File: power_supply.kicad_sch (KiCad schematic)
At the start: 48 parts, among them J1 USB_C_Receptacle_USB2.0, Q2 IRLR3110ZTRPBF, Q3 BSR92P, Q4 BSR92P, Q5 BSS131, Q6 BSS131, Q7 BSS131, Q8 BSS131, U1 LT3757AEMSE, U2 AMS1117-3.3

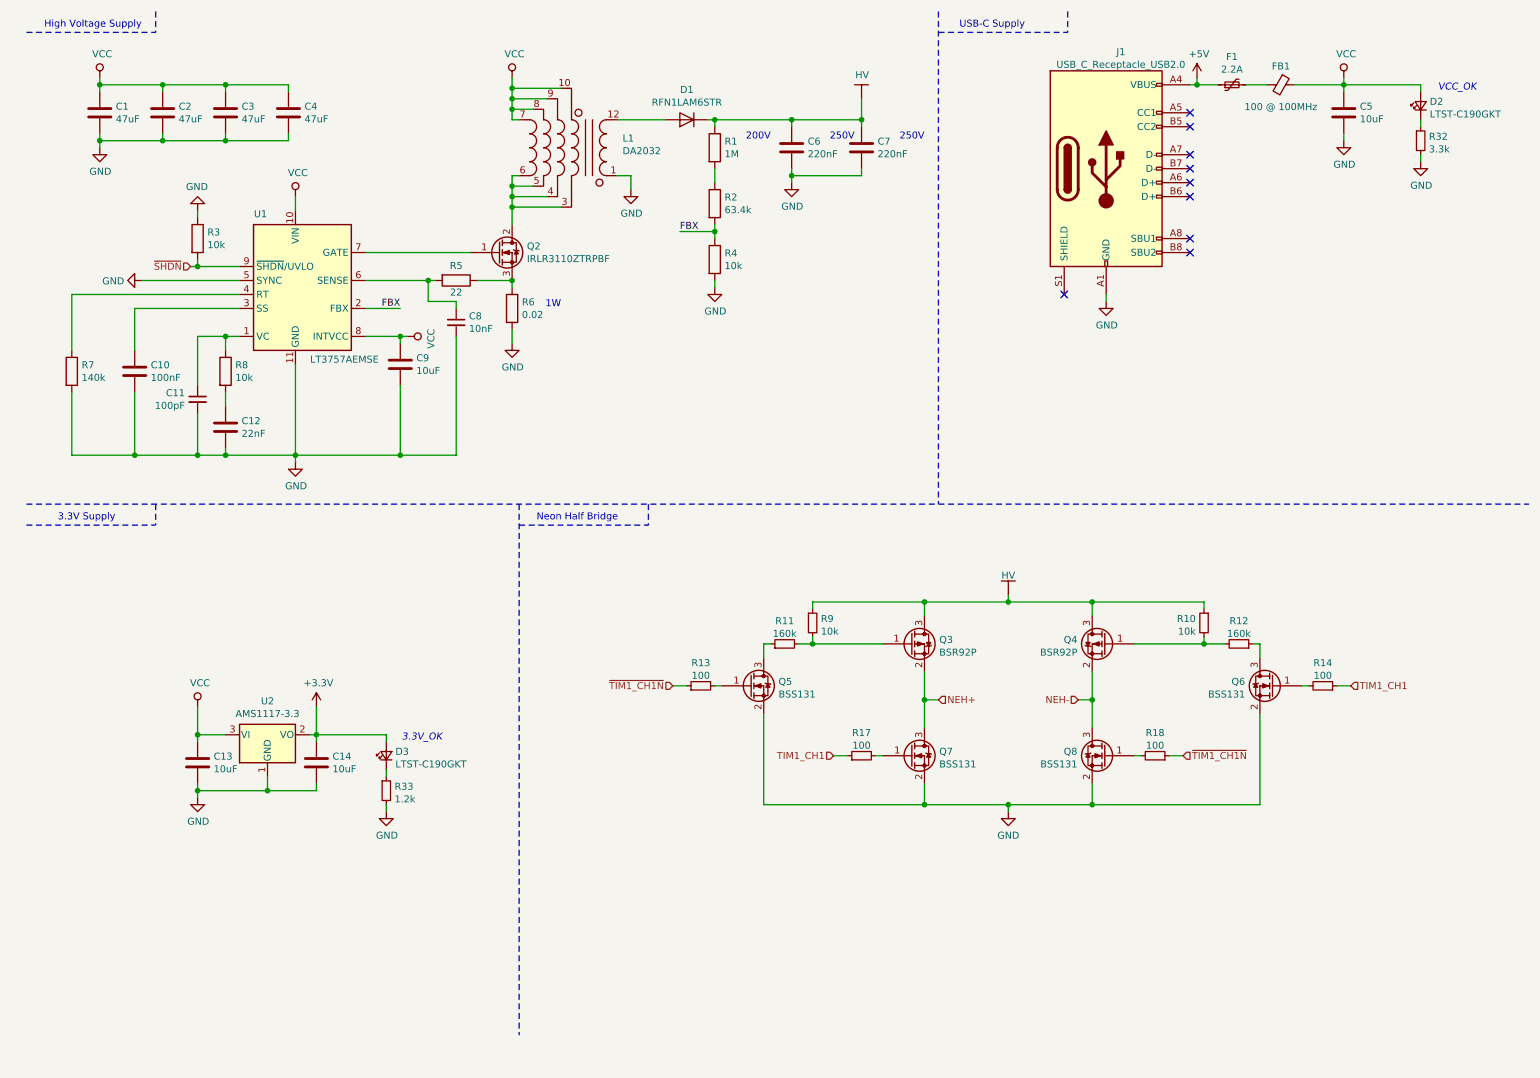
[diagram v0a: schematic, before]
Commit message: added outputs for schematic and gerber view
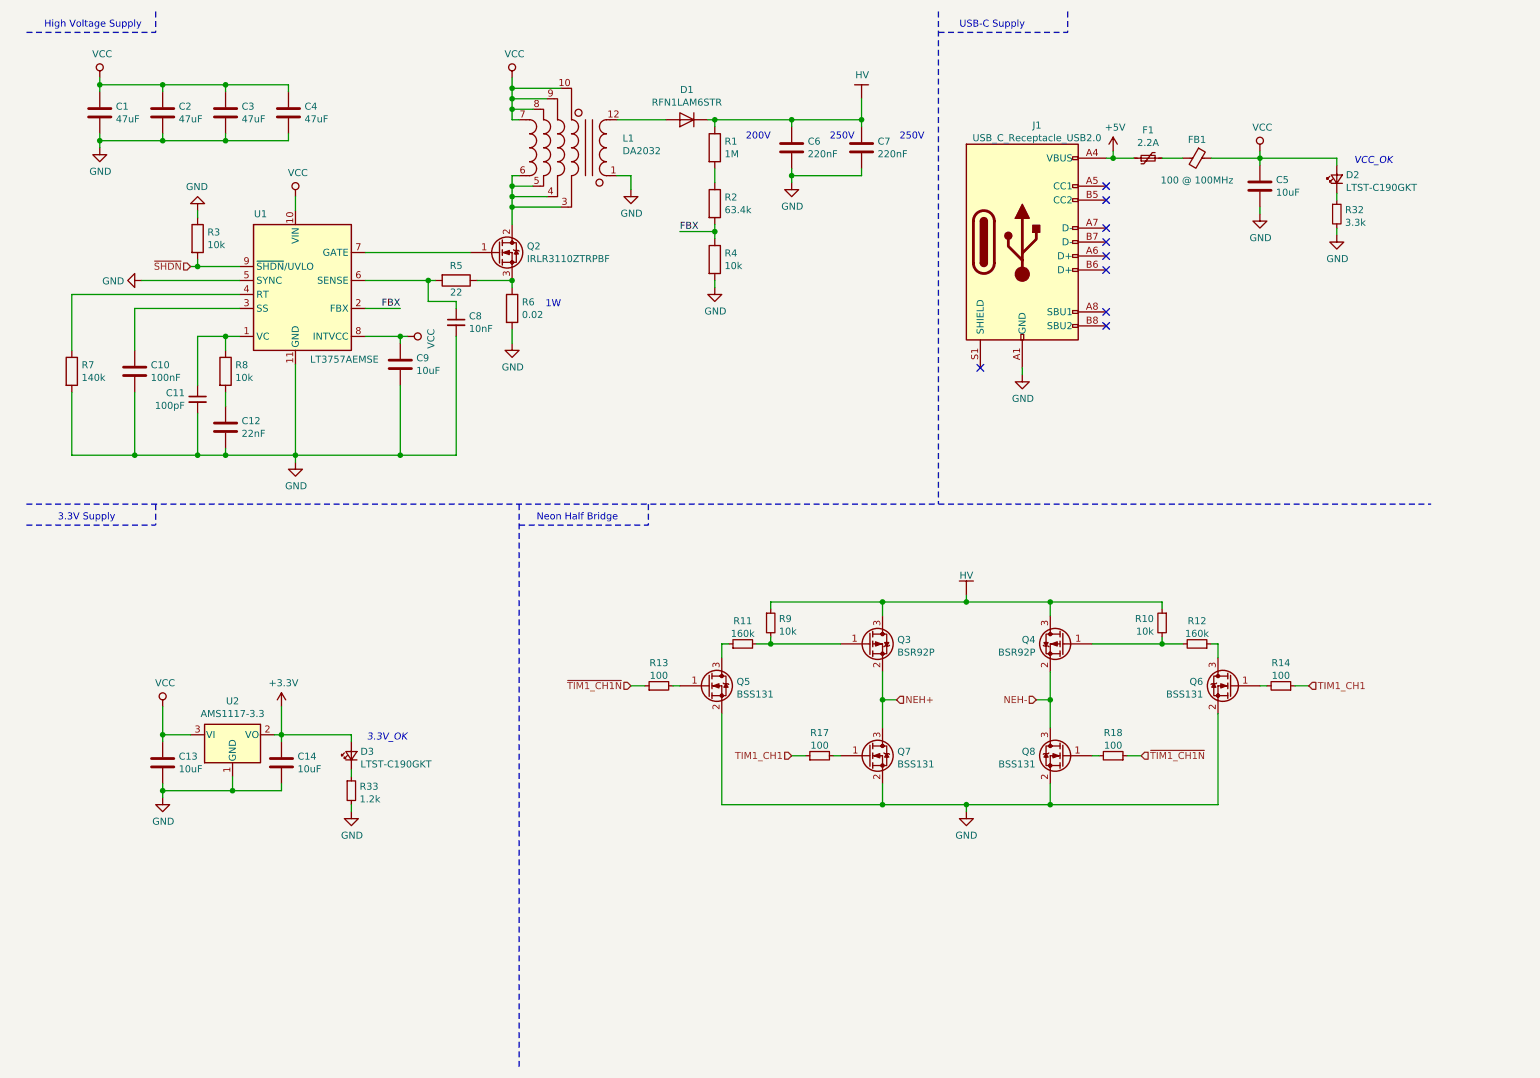
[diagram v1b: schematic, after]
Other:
- moved on the sheet: C13, C14, C5, D2, D3, F1, FB1, J1, Q3, Q4, Q5, Q6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

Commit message: finalized design; fixed NE-2 bulb work
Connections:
- net HV: now also Q3.2 (S), Q4.2 (S); no longer Q3.3 (D), Q4.3 (D)
- net NEH+: now also Q3.3 (D); no longer Q3.2 (S)
- net NEH-: now also Q4.3 (D); no longer Q4.2 (S)
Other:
- moved on the sheet: Q4
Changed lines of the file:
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@@
   (title_block
     (title "Nixie Clock - Power Supply")
-    (date "2021-03-24")
-    (rev "20210324")
+    (date "2021-06-06")
+    (rev "20210606")
     (company "Bastian de Byl")
     (comment 1 "QC: OK")
@@
     (pin "3")
   )
-  (symbol (lib_id "Device:Q_PMOS_GSD") (at 165.1 127 0) (unit 1)
-    (in_bom yes) (on_board yes)
-    (property "Reference" "Q3" (id 0) (at 170.3325 126.2391 0)
-      (effects (font (size 1.27 1.27)) (justify left))
-    )
-    (property "Value" "BSR92P" (id 1) (at 170.3325 128.5378 0)
-      (effects (font (size 1.27 1.27)) (justify left))
-    )
-    (property "Footprint" "Package_TO_SOT_SMD:SOT-23" (id 2) (at 170.18 124.46 0)
+  (symbol (lib_id "Device:Q_PMOS_GSD") (at 165.1 127 0) (mirror x) (unit 1)
+    (in_bom yes) (on_board yes)
+    (property "Reference" "Q3" (id 0) (at 170.3325 127.7609 0)
+      (effects (font (size 1.27 1.27)) (justify left))
+    )
+    (property "Value" "BSR92P" (id 1) (at 170.3325 125.4622 0)
+      (effects (font (size 1.27 1.27)) (justify left))
+    )
+    (property "Footprint" "Package_TO_SOT_SMD:SOT-23" (id 2) (at 170.18 129.54 0)
       (effects (font (size 1.27 1.27)) hide)
     )
@@
     (pin "3")
   )
-  (symbol (lib_id "Device:Q_PMOS_GSD") (at 200.66 127 0) (mirror y) (unit 1)
-    (in_bom yes) (on_board yes)
-    (property "Reference" "Q4" (id 0) (at 195.4275 126.2391 0)
-      (effects (font (size 1.27 1.27)) (justify left))
-    )
-    (property "Value" "BSR92P" (id 1) (at 195.4275 128.5378 0)
-      (effects (font (size 1.27 1.27)) (justify left))
-    )
-    (property "Footprint" "Package_TO_SOT_SMD:SOT-23" (id 2) (at 195.58 124.46 0)
-      (effects (font (size 1.27 1.27)) hide)
-    )
+  (symbol (lib_id "Device:Q_PMOS_GSD") (at 200.66 127 180) (unit 1)
+    (in_bom yes) (on_board yes)
+    (property "Reference" "Q4" (id 0) (at 195.4275 127.7609 0)
+      (effects (font (size 1.27 1.27)) (justify left))
+    )
+    (property "Value" "BSR92P" (id 1) (at 195.4275 125.4622 0)
+      (effects (font (size 1.27 1.27)) (justify left))
+    )
+    (property "Footprint" "Package_TO_SOT_SMD:SOT-23" (id 2) (at 195.58 129.54 0)
+      (effects (font (size 1.27 1.27)) hide)
+    )
